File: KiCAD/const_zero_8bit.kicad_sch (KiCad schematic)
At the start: 0 parts

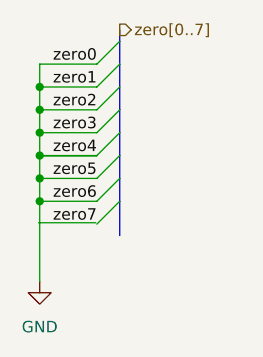
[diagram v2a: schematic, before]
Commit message: fix multiple ERCs that made RAM addrs not connecting
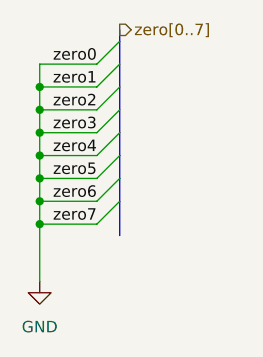
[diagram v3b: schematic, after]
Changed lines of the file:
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@@
 	(paper "A4")
 	(junction
+		(at 207.01 101.6)
+		(diameter 0)
+		(color 0 0 0 0)
+	)
+	(junction
 		(at 207.01 96.52)
 		(diameter 0)
@@
 	)
 	(junction
+		(at 207.01 93.98)
+		(diameter 0)
+		(color 0 0 0 0)
+	)
+	(junction
 		(at 207.01 91.44)
 		(diameter 0)
@@
 	)
 	(junction
-		(at 207.01 93.98)
-		(diameter 0)
-		(color 0 0 0 0)
-	)
-	(junction
 		(at 207.01 88.9)
 		(diameter 0)
@@
 		)
 	)
+	(wire
+		(pts
+			(xy 207.01 96.52) (xy 207.01 99.06)
+		)
+		(stroke
+			(width 0)
+			(type default)
+		)
+	)
+	(wire
+		(pts
+			(xy 207.01 83.82) (xy 207.01 86.36)
+		)
+		(stroke
+			(width 0)
+			(type default)
+		)
+	)
 	(bus
 		(pts
@@
 		)
 	)
+	(bus
+		(pts
+			(xy 215.9 96.52) (xy 215.9 99.06)
+		)
+		(stroke
+			(width 0)
+			(type default)
+		)
+	)
+	(bus
+		(pts
+			(xy 215.9 91.44) (xy 215.9 93.98)
+		)
+		(stroke
+			(width 0)
+			(type default)
+		)
+	)
+	(wire
+		(pts
+			(xy 207.01 86.36) (xy 207.01 88.9)
+		)
+		(stroke
+			(width 0)
+			(type default)
+		)
+	)
+	(wire
+		(pts
+			(xy 207.01 96.52) (xy 213.36 96.52)
+		)
+		(stroke
+			(width 0)
+			(type default)
+		)
+	)
+	(bus
+		(pts
+			(xy 215.9 83.82) (xy 215.9 86.36)
+		)
+		(stroke
+			(width 0)
+			(type default)
+		)
+	)
+	(bus
+		(pts
+			(xy 215.9 93.98) (xy 215.9 96.52)
+		)
+		(stroke
+			(width 0)
+			(type default)
+		)
+	)
+	(wire
+		(pts
+			(xy 207.01 99.06) (xy 213.36 99.06)
+		)
+		(stroke
+			(width 0)
+			(type default)
+		)
+	)
+	(wire
+		(pts
+			(xy 207.01 93.98) (xy 213.36 93.98)
+		)
+		(stroke
+			(width 0)
+			(type default)
+		)
+	)
+	(wire
+		(pts
+			(xy 207.01 101.6) (xy 207.01 107.95)
+		)
+		(stroke
+			(width 0)
+			(type default)
+		)
+	)
+	(bus
+		(pts
+			(xy 215.9 80.01) (xy 215.9 81.28)
+		)
+		(stroke
+			(width 0)
+			(type default)
+		)
+	)
+	(wire
+		(pts
+			(xy 207.01 88.9) (xy 207.01 91.44)
+		)
+		(stroke
+			(width 0)
+			(type default)
+		)
+	)
+	(wire
+		(pts
+			(xy 207.01 86.36) (xy 213.36 86.36)
+		)
+		(stroke
+			(width 0)
+			(type default)
+		)
+	)
+	(bus
+		(pts
+			(xy 215.9 86.36) (xy 215.9 88.9)
+		)
+		(stroke
+			(width 0)
+			(type default)
+		)
+	)
+	(bus
+		(pts
+			(xy 215.9 99.06) (xy 215.9 102.87)
+		)
+		(stroke
+			(width 0)
+			(type default)
+		)
+	)
+	(wire
+		(pts
+			(xy 207.01 101.6) (xy 213.36 101.6)
+		)
+		(stroke
+			(width 0)
+			(type default)
+		)
+	)
 	(wire
 		(pts
@@
 		)
 	)
+	(bus
+		(pts
+			(xy 215.9 81.28) (xy 215.9 83.82)
+		)
+		(stroke
+			(width 0)
+			(type default)
+		)
+	)
+	(wire
+		(pts
+			(xy 207.01 99.06) (xy 207.01 101.6)
+		)
+		(stroke
+			(width 0)
+			(type default)
+		)
+	)
+	(wire
+		(pts
+			(xy 207.01 83.82) (xy 213.36 83.82)
+		)
+		(stroke
+			(width 0)
+			(type default)
+		)
+	)
+	(wire
+		(pts
+			(xy 207.01 91.44) (xy 213.36 91.44)
+		)
+		(stroke
+			(width 0)
+			(type default)
+		)
+	)
 	(wire
 		(pts
@@
 		)
 		(stroke
-			(width 0)
-			(type default)
-		)
-	)
-	(wire
-		(pts
-			(xy 207.01 96.52) (xy 207.01 99.06)
-		)
-		(stroke
-			(width 0)
-			(type default)
-		)
-	)
-	(wire
-		(pts
-			(xy 207.01 83.82) (xy 207.01 86.36)
-		)
-		(stroke
-			(width 0)
-			(type default)
-		)
-	)
-	(bus
-		(pts
-			(xy 215.9 96.52) (xy 215.9 99.06)
-		)
-		(stroke
-			(width 0)
-			(type default)
-		)
-	)
-	(bus
-		(pts
-			(xy 215.9 91.44) (xy 215.9 93.98)
-		)
-		(stroke
-			(width 0)
-			(type default)
-		)
-	)
-	(wire
-		(pts
-			(xy 207.01 86.36) (xy 207.01 88.9)
-		)
-		(stroke
-			(width 0)
-			(type default)
-		)
-	)
-	(wire
-		(pts
-			(xy 207.01 96.52) (xy 213.36 96.52)
-		)
-		(stroke
-			(width 0)
-			(type default)
-		)
-	)
-	(bus
-		(pts
-			(xy 215.9 83.82) (xy 215.9 86.36)
-		)
-		(stroke
-			(width 0)
-			(type default)
-		)
-	)
-	(bus
-		(pts
-			(xy 215.9 93.98) (xy 215.9 96.52)
-		)
-		(stroke
-			(width 0)
-			(type default)
-		)
-	)
-	(bus
-		(pts
-			(xy 215.9 86.36) (xy 215.9 88.9)
-		)
-		(stroke
-			(width 0)
-			(type default)
-		)
-	)
-	(wire
-		(pts
-			(xy 207.01 99.06) (xy 213.36 99.06)
-		)
-		(stroke
-			(width 0)
-			(type default)
-		)
-	)
-	(bus
-		(pts
-			(xy 215.9 80.01) (xy 215.9 81.28)
-		)
-		(stroke
-			(width 0)
-			(type default)
-		)
-	)
-	(wire
-		(pts
-			(xy 207.01 93.98) (xy 213.36 93.98)
-		)
-		(stroke
-			(width 0)
-			(type default)
-		)
-	)
-	(wire
-		(pts
-			(xy 207.01 88.9) (xy 207.01 91.44)
-		)
-		(stroke
-			(width 0)
-			(type default)
-		)
-	)
-	(wire
-		(pts
-			(xy 207.01 86.36) (xy 213.36 86.36)
-		)
-		(stroke
-			(width 0)
-			(type default)
-		)
-	)
-	(wire
-		(pts
-			(xy 206.9968 94.0099) (xy 213.3468 94.0099)
-		)
-		(stroke
-			(width 0)
-			(type default)
-		)
-	)
-	(bus
-		(pts
-			(xy 215.9 99.06) (xy 215.9 102.87)
-		)
-		(stroke
-			(width 0)
-			(type default)
-		)
-	)
-	(wire
-		(pts
-			(xy 206.8836 101.4448) (xy 213.2336 101.4448)
-		)
-		(stroke
-			(width 0)
-			(type default)
-		)
-	)
-	(wire
-		(pts
-			(xy 207.01 91.44) (xy 213.36 91.44)
-		)
-		(stroke
-			(width 0)
-			(type default)
-		)
-	)
-	(bus
-		(pts
-			(xy 215.9 81.28) (xy 215.9 83.82)
-		)
-		(stroke
-			(width 0)
-			(type default)
-		)
-	)
-	(wire
-		(pts
-			(xy 207.01 99.06) (xy 207.01 107.95)
-		)
-		(stroke
-			(width 0)
-			(type default)
-		)
-	)
-	(wire
-		(pts
-			(xy 207.01 83.82) (xy 213.36 83.82)
-		)
-		(stroke
